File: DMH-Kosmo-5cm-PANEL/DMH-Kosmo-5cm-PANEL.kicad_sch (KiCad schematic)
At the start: 5 parts, among them J0 Panel_GND_Solder_Wire_Pad

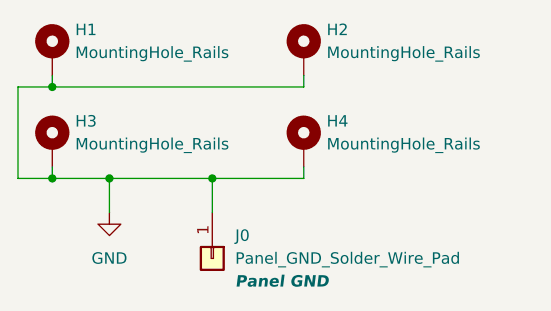
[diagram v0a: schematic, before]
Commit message: Changed panel GND pad function to just GND
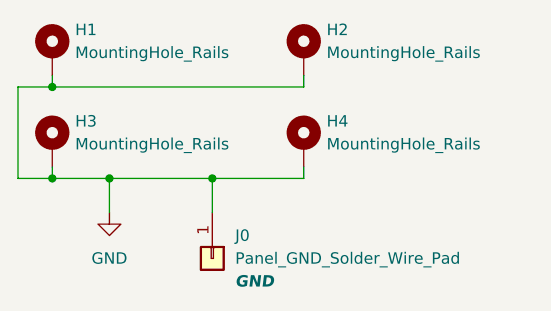
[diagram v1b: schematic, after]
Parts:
- J0: Function Panel GND -> GND
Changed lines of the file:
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@@
 			)
 		)
-		(property "Function" "Panel GND"
+		(property "Function" "GND"
 			(at 48.26 280.67 90)
 			(effects
